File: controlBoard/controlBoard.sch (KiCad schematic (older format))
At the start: 32 parts, among them J1 FTDI, J2 Servo, J3 Fingerprint, J4 Barrel_Jack_Switch, J5 ICSP, SW1 SW_Push, SW2 SW_Push, SW3 SW_Push, U1 ATmega328P-AU, U2 PCA9685BS, U3 AP2112K-3.3TRG1, Y1 Crystal

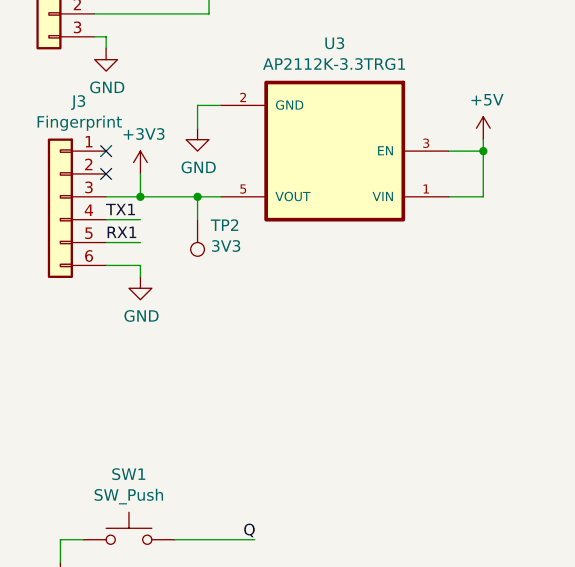
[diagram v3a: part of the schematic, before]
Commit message: Added decoupling cap for fingerprint reader, generated gerbers
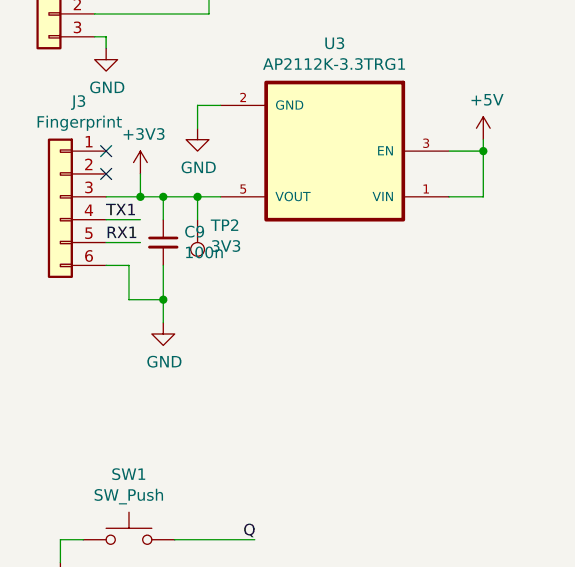
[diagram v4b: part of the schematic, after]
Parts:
- added C9: 100n, Capacitor_SMD:C_0805_2012Metric_Pad1.18x1.45mm_HandSolder, symbol Device:C_Small
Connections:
- wire segments 153 -> 158
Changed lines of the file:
@@
-$EndComp
-$Comp
-L controlBoard-rescue:GND-power #PWR011
-U 1 1 618F500B
-P 1750 1800
-F 0 "#PWR011" H 1750 1550 50  0001 C CNN
-F 1 "GND" H 1755 1627 50  0000 C CNN
-F 2 "" H 1750 1800 50  0001 C CNN
-F 3 "" H 1750 1800 50  0001 C CNN
-	1    1750 1800
-	1    0    0    -1
 $EndComp
 $Comp
@@
 RX1
 $Comp
-L controlBoard-rescue:GND-power #PWR03
-U 1 1 6199143D
-P 1300 2750
-F 0 "#PWR03" H 1300 2500 50  0001 C CNN
-F 1 "GND" H 1305 2577 50  0000 C CNN
-F 2 "" H 1300 2750 50  0001 C CNN
-F 3 "" H 1300 2750 50  0001 C CNN
-	1    1300 2750
-	1    0    0    -1
-$EndComp
-Wire Wire Line
-	1250 2700 1300 2700
-Wire Wire Line
-	1300 2700 1300 2750
-Wire Wire Line
-	1250 2300 1400 2300
-Wire Wire Line
-	1250 2400 1400 2400
-Text Label 1300 2300 0    50   ~ 0
-TX
-Text Label 1300 2400 0    50   ~ 0
-RX
-$Comp
-L controlBoard-rescue:+5V-power #PWR09
-U 1 1 6199F7F4
-P 1750 2450
-F 0 "#PWR09" H 1750 2300 50  0001 C CNN
-F 1 "+5V" H 1765 2623 50  0000 C CNN
-F 2 "" H 1750 2450 50  0001 C CNN
-F 3 "" H 1750 2450 50  0001 C CNN
-	1    1750 2450
-	1    0    0    -1
-$EndComp
-Wire Wire Line
-	1250 2600 1400 2600
-Text Label 1650 2200 0    50   ~ 0
-RESET
-Wire Wire Line
-	1600 2200 1900 2200
-$Comp
 L controlBoard-rescue:C_Small-device C6
 U 1 1 618FF053
@@
 $EndComp
 $Comp
-L controlBoard-rescue:SolderJumper_2_Open-Jumper JP1
-U 1 1 61BD91B4
-P 1550 2500
-F 0 "JP1" H 1550 2705 50  0000 C CNN
-F 1 "JVCC" H 1550 2614 50  0000 C CNN
-F 2 "Jumper:SolderJumper-2_P1.3mm_Open_RoundedPad1.0x1.5mm" H 1550 2500 50  0001 C CNN
-F 3 "~" H 1550 2500 50  0001 C CNN
-	1    1550 2500
-	1    0    0    -1
-$EndComp
-Wire Wire Line
-	1250 2500 1400 2500
-$Comp
-L controlBoard-rescue:C_Small-Device C1
-U 1 1 61BF76F9
-P 1500 2200
-F 0 "C1" V 1271 2200 50  0000 C CNN
-F 1 "100n" V 1362 2200 50  0000 C CNN
-F 2 "Capacitor_SMD:C_0805_2012Metric_Pad1.18x1.45mm_HandSolder" H 1500 2200 50  0001 C CNN
-F 3 "~" H 1500 2200 50  0001 C CNN
-	1    1500 2200
-	0    1    1    0
-$EndComp
-Wire Wire Line
-	1400 2200 1250 2200
-Wire Wire Line
-	1700 2500 1750 2500
-Wire Wire Line
-	1750 2500 1750 2450
-$Comp
 L controlBoard-rescue:C_Small-Device C2
 U 1 1 61C0D1ED
@@
 Wire Wire Line
 	3200 2600 3300 2600
-$Comp
-L controlBoard-rescue:Conn_01x06-Connector_Generic J1
-U 1 1 618EBBB2
-P 1050 2500
-F 0 "J1" H 968 1975 50  0000 C CNN
-F 1 "FTDI" H 968 2066 50  0000 C CNN
-F 2 "Connector_PinHeader_2.54mm:PinHeader_1x06_P2.54mm_Vertical" H 1050 2500 50  0001 C CNN
-F 3 "~" H 1050 2500 50  0001 C CNN
-	1    1050 2500
-	-1   0    0    1
-$EndComp
 Wire Wire Line
 	1550 6750 1900 6750
@@
 L controlBoard-rescue:GND-power #PWR06
 U 1 1 6197312B
-P 1400 4550
-F 0 "#PWR06" H 1400 4300 50  0001 C CNN
-F 1 "GND" H 1405 4377 50  0000 C CNN
-F 2 "" H 1400 4550 50  0001 C CNN
-F 3 "" H 1400 4550 50  0001 C CNN
-	1    1400 4550
-	1    0    0    -1
-$EndComp
-Wire Wire Line
-	1400 4500 1400 4550
-Wire Wire Line
-	1250 4500 1400 4500
+P 1500 4750
+F 0 "#PWR06" H 1500 4500 50  0001 C CNN
+F 1 "GND" H 1505 4577 50  0000 C CNN
+F 2 "" H 1500 4750 50  0001 C CNN
+F 3 "" H 1500 4750 50  0001 C CNN
+	1    1500 4750
+	1    0    0    -1
+$EndComp
 Wire Wire Line
 	1250 4300 1400 4300
@@
 Connection ~ 1400 4200
 Wire Wire Line
-	1400 4200 1650 4200
+	1400 4200 1500 4200
 $Comp
 L Connector:TestPoint TP2
@@
 Wire Wire Line
 	6450 3000 7050 3000
+$Comp
+L controlBoard-rescue:Conn_01x06-Connector_Generic J1
+U 1 1 618EBBB2
+P 1050 2500
+F 0 "J1" H 968 1975 50  0000 C CNN
+F 1 "FTDI" H 968 2066 50  0000 C CNN
+F 2 "Connector_PinHeader_2.54mm:PinHeader_1x06_P2.54mm_Vertical" H 1050 2500 50  0001 C CNN
+F 3 "~" H 1050 2500 50  0001 C CNN
+	1    1050 2500
+	-1   0    0    1
+$EndComp
+Wire Wire Line
+	1750 2500 1750 2450
+Wire Wire Line
+	1700 2500 1750 2500
+Wire Wire Line
+	1400 2200 1250 2200
+$Comp
+L controlBoard-rescue:C_Small-Device C1
+U 1 1 61BF76F9
+P 1500 2200
+F 0 "C1" V 1271 2200 50  0000 C CNN
+F 1 "100n" V 1362 2200 50  0000 C CNN
+F 2 "Capacitor_SMD:C_0805_2012Metric_Pad1.18x1.45mm_HandSolder" H 1500 2200 50  0001 C CNN
+F 3 "~" H 1500 2200 50  0001 C CNN
+	1    1500 2200
+	0    1    1    0
+$EndComp
+Wire Wire Line
+	1250 2500 1400 2500
+$Comp
+L controlBoard-rescue:SolderJumper_2_Open-Jumper JP1
+U 1 1 61BD91B4
+P 1550 2500
+F 0 "JP1" H 1550 2705 50  0000 C CNN
+F 1 "JVCC" H 1550 2614 50  0000 C CNN
+F 2 "Jumper:SolderJumper-2_P1.3mm_Open_RoundedPad1.0x1.5mm" H 1550 2500 50  0001 C CNN
+F 3 "~" H 1550 2500 50  0001 C CNN
+	1    1550 2500
+	1    0    0    -1
+$EndComp
+Wire Wire Line
+	1600 2200 1900 2200
+Text Label 1650 2200 0    50   ~ 0
+RESET
+Wire Wire Line
+	1250 2600 1400 2600
+$Comp
+L controlBoard-rescue:+5V-power #PWR09
+U 1 1 6199F7F4
+P 1750 2450
+F 0 "#PWR09" H 1750 2300 50  0001 C CNN
+F 1 "+5V" H 1765 2623 50  0000 C CNN
+F 2 "" H 1750 2450 50  0001 C CNN
+F 3 "" H 1750 2450 50  0001 C CNN
+	1    1750 2450
+	1    0    0    -1
+$EndComp
+Text Label 1300 2400 0    50   ~ 0
+RX
+Text Label 1300 2300 0    50   ~ 0
+TX
+Wire Wire Line
+	1250 2400 1400 2400
+Wire Wire Line
+	1250 2300 1400 2300
+Wire Wire Line
+	1300 2700 1300 2750
+Wire Wire Line
+	1250 2700 1300 2700
+$Comp
+L controlBoard-rescue:GND-power #PWR03
+U 1 1 6199143D
+P 1300 2750
+F 0 "#PWR03" H 1300 2500 50  0001 C CNN
+F 1 "GND" H 1305 2577 50  0000 C CNN
+F 2 "" H 1300 2750 50  0001 C CNN
+F 3 "" H 1300 2750 50  0001 C CNN
+	1    1300 2750
+	1    0    0    -1
+$EndComp
+$Comp
+L controlBoard-rescue:GND-power #PWR011
+U 1 1 618F500B
+P 1750 1800
+F 0 "#PWR011" H 1750 1550 50  0001 C CNN
+F 1 "GND" H 1755 1627 50  0000 C CNN
+F 2 "" H 1750 1800 50  0001 C CNN
+F 3 "" H 1750 1800 50  0001 C CNN
+	1    1750 1800
+	1    0    0    -1
+$EndComp
+$Comp
+L Device:C_Small C9
+U 1 1 61DF6837
+P 1500 4400
+F 0 "C9" H 1592 4446 50  0000 L CNN
+F 1 "100n" H 1592 4355 50  0000 L CNN
+F 2 "Capacitor_SMD:C_0805_2012Metric_Pad1.18x1.45mm_HandSolder" H 1500 4400 50  0001 C CNN
+F 3 "~" H 1500 4400 50  0001 C CNN
+	1    1500 4400
+	1    0    0    -1
+$EndComp
+Wire Wire Line
+	1500 4500 1500 4650
+Wire Wire Line
+	1250 4500 1350 4500
+Wire Wire Line
+	1350 4500 1350 4650
+Wire Wire Line
+	1350 4650 1500 4650
+Connection ~ 1500 4650
+Wire Wire Line
+	1500 4650 1500 4750
+Wire Wire Line
+	1500 4300 1500 4200
+Connection ~ 1500 4200
+Wire Wire Line
+	1500 4200 1650 4200
 $EndSCHEMATC
